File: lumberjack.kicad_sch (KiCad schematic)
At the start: 180 parts, among them J1 USB, J2 AVR_ISP_6, J3 JST, J4 JST, SW1 RESET, SW2 BOOT, U2 ATmega32A-P, Y1 16MHz

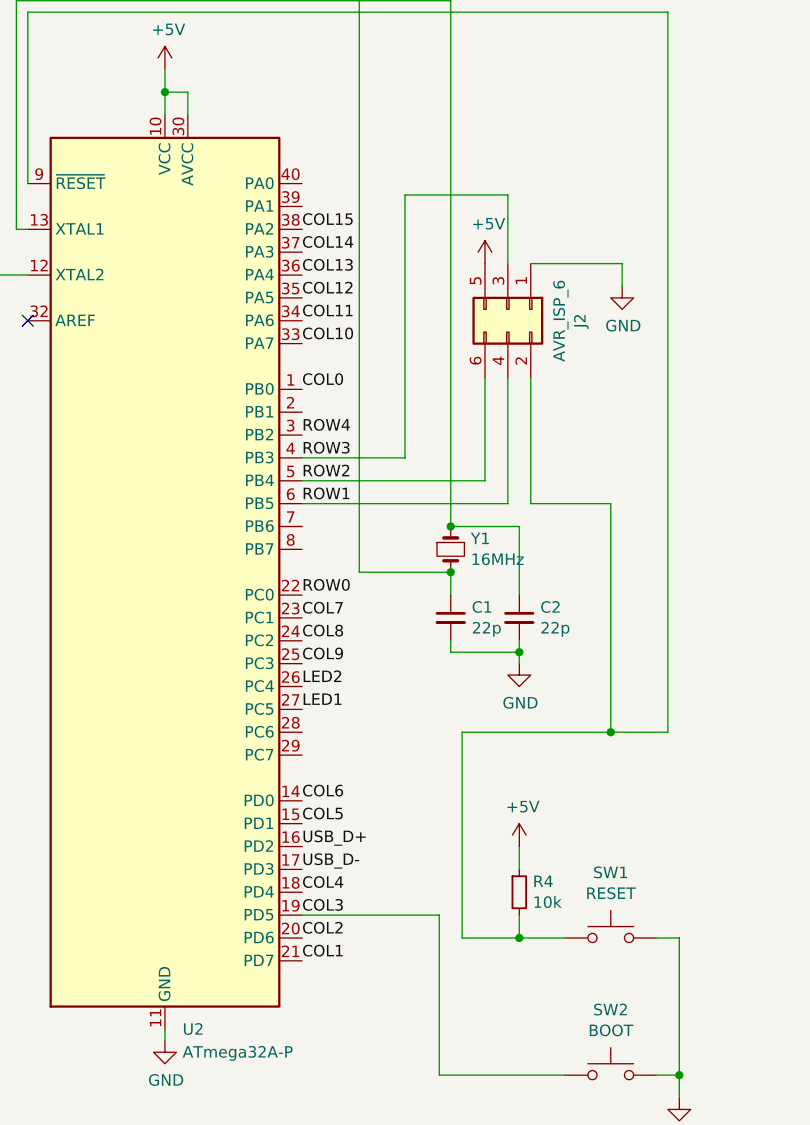
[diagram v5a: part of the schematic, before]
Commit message: middle part layout and traces
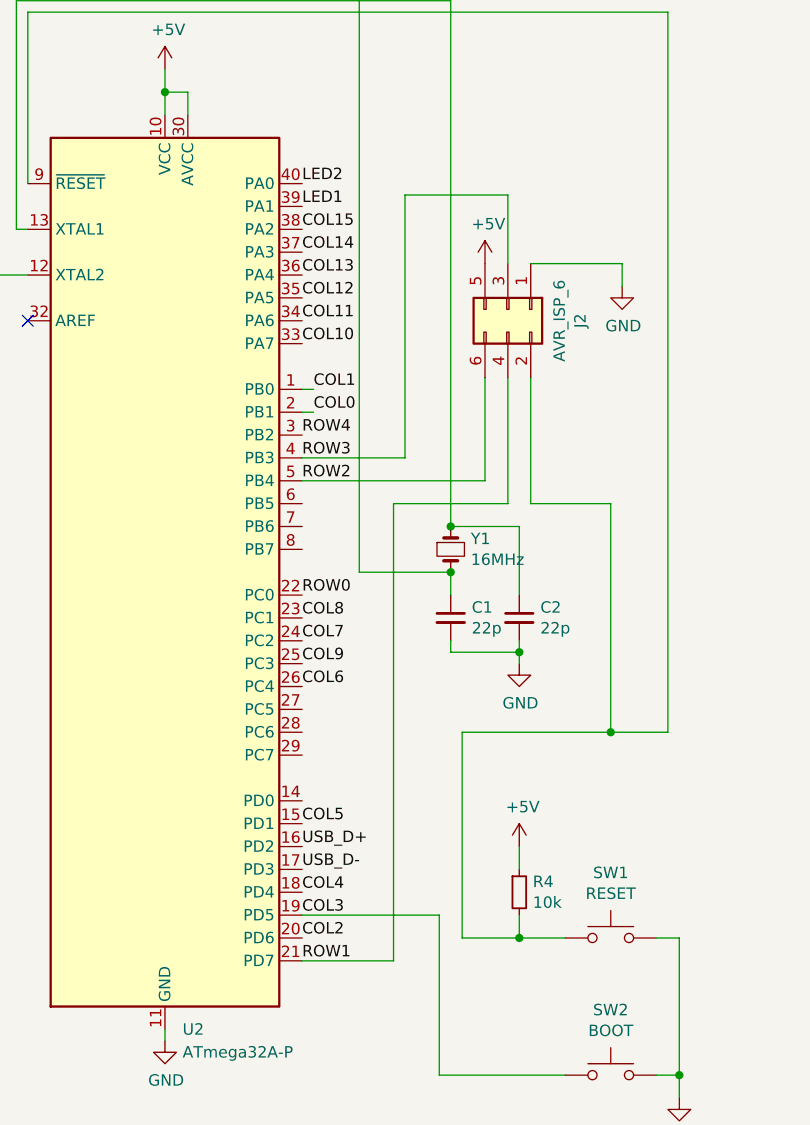
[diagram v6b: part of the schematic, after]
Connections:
- net COL0: now also U2.2 (PB1); no longer U2.1 (PB0)
- net COL1: now also U2.1 (PB0); no longer U2.21 (PD7)
- net COL6: now also U2.26 (PC4); no longer U2.14 (PD0)
- net COL7: now also U2.24 (PC2); no longer U2.23 (PC1)
- net COL8: now also U2.23 (PC1); no longer U2.24 (PC2)
- net LED1: now also U2.39 (PA1); no longer U2.27 (PC5)
- net LED2: now also U2.40 (PA0); no longer U2.26 (PC4)
- net ROW1: now also U2.21 (PD7); no longer U2.6 (PB5)
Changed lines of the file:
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@@
+    (stroke (width 0) (type default))
+  )
+  (wire (pts (xy 64.77 146.05) (xy 64.77 196.85))
     (stroke (width 0) (type default))
   )
@@
     (stroke (width 0) (type default))
   )
+  (wire (pts (xy 55.88 135.89) (xy 54.61 135.89))
+    (stroke (width 0) (type default))
+  )
   (wire (pts (xy 67.31 64.77) (xy 59.69 64.77))
     (stroke (width 0) (type default))
@@
     (stroke (width 0) (type default))
   )
-  (wire (pts (xy 54.61 146.05) (xy 77.47 146.05))
+  (wire (pts (xy 77.47 146.05) (xy 64.77 146.05))
     (stroke (width 0) (type default))
   )
@@
     (stroke (width 0) (type default))
   )
+  (wire (pts (xy 55.88 133.35) (xy 54.61 133.35))
+    (stroke (width 0) (type default))
+  )
   (wire (pts (xy 69.85 209.55) (xy 83.82 209.55))
     (stroke (width 0) (type default))
@@
   )
   (wire (pts (xy 302.26 74.93) (xy 302.26 92.71))
+    (stroke (width 0) (type default))
+  )
+  (wire (pts (xy 64.77 196.85) (xy 54.61 196.85))
     (stroke (width 0) (type default))
   )
@@
     (effects (font (size 1.27 1.27)) (justify left bottom))
   )
-  (label "COL1" (at 54.61 196.85 0) (fields_autoplaced)
+  (label "COL1" (at 55.88 133.35 0) (fields_autoplaced)
     (effects (font (size 1.27 1.27)) (justify left bottom))
   )
@@
     (effects (font (size 1.27 1.27)) (justify left bottom))
   )
-  (label "LED2" (at 54.61 166.37 0) (fields_autoplaced)
+  (label "LED2" (at 54.61 110.49 0) (fields_autoplaced)
     (effects (font (size 1.27 1.27)) (justify left bottom))
   )
@@
     (effects (font (size 1.27 1.27)) (justify left bottom))
   )
-  (label "LED1" (at 54.61 168.91 0) (fields_autoplaced)
+  (label "LED1" (at 54.61 113.03 0) (fields_autoplaced)
     (effects (font (size 1.27 1.27)) (justify left bottom))
   )
@@
     (effects (font (size 1.27 1.27)) (justify right bottom))
   )
-  (label "COL8" (at 54.61 161.29 0) (fields_autoplaced)
+  (label "COL8" (at 54.61 158.75 0) (fields_autoplaced)
     (effects (font (size 1.27 1.27)) (justify left bottom))
   )
@@
     (effects (font (size 1.27 1.27)) (justify left bottom))
   )
-  (label "COL6" (at 54.61 179.07 0) (fields_autoplaced)
+  (label "COL6" (at 54.61 166.37 0) (fields_autoplaced)
     (effects (font (size 1.27 1.27)) (justify left bottom))
   )
@@
     (effects (font (size 1.27 1.27)) (justify right bottom))
   )
-  (label "COL7" (at 54.61 158.75 0) (fields_autoplaced)
+  (label "COL7" (at 54.61 161.29 0) (fields_autoplaced)
     (effects (font (size 1.27 1.27)) (justify left bottom))
   )
@@
     (effects (font (size 1.27 1.27)) (justify left bottom))
   )
-  (label "ROW1" (at 54.61 146.05 0) (fields_autoplaced)
+  (label "ROW1" (at 54.61 196.85 0) (fields_autoplaced)
     (effects (font (size 1.27 1.27)) (justify left bottom))
   )
@@
     (effects (font (size 1.27 1.27)) (justify left bottom))
   )
-  (label "COL0" (at 54.61 133.35 0) (fields_autoplaced)
-    (effects (font (size 1.27 1.27)) (justify left bottom))
-  )
+  (label "COL0" (at 55.88 135.89 0) (fields_autoplaced)
+    (effects (font (size 1.27 1.27)) (justify left bottom))
+  )

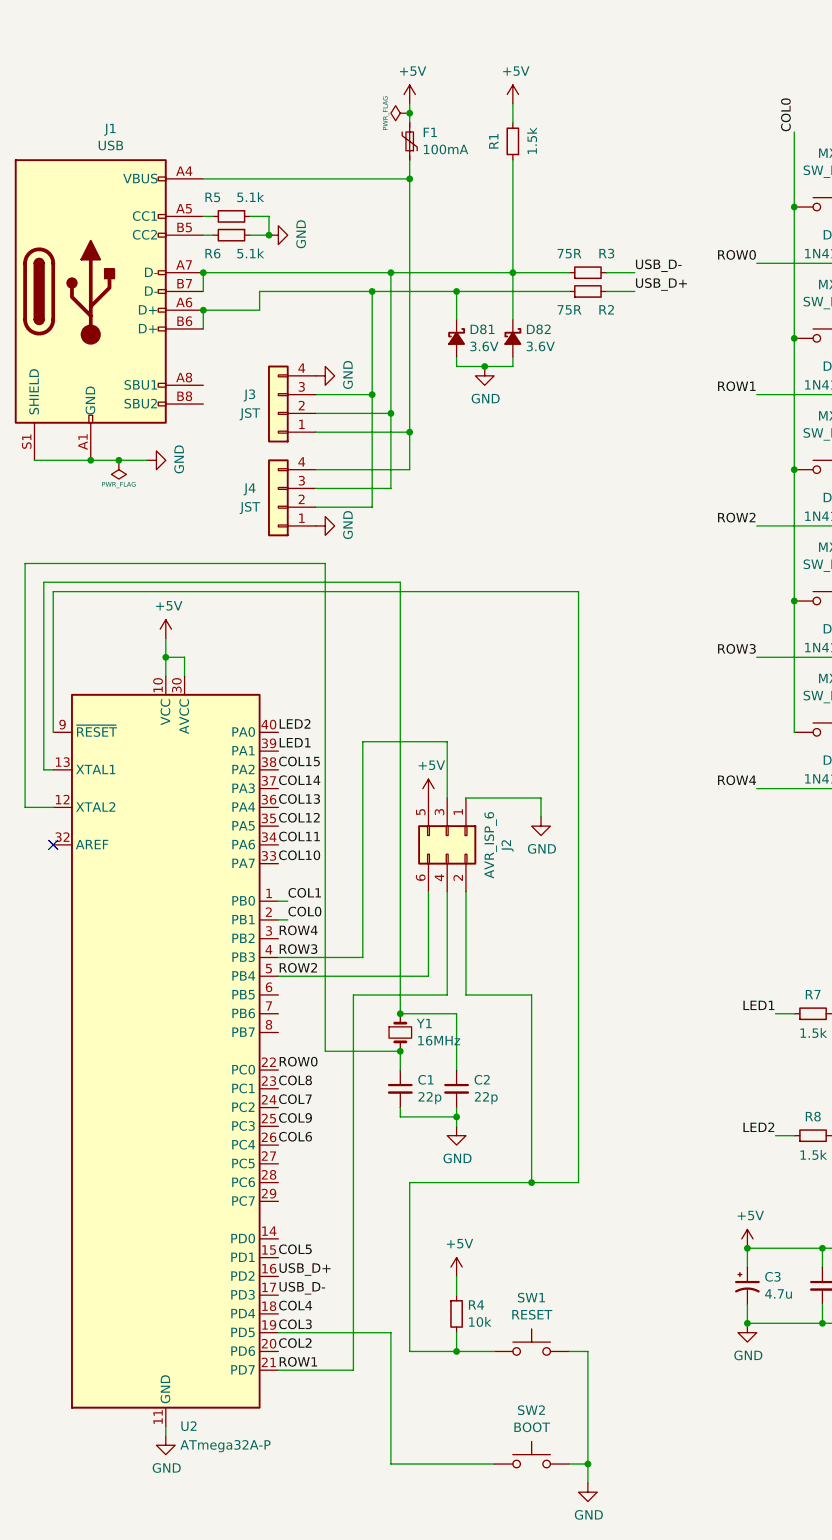
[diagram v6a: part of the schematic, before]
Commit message: usb mini and traces
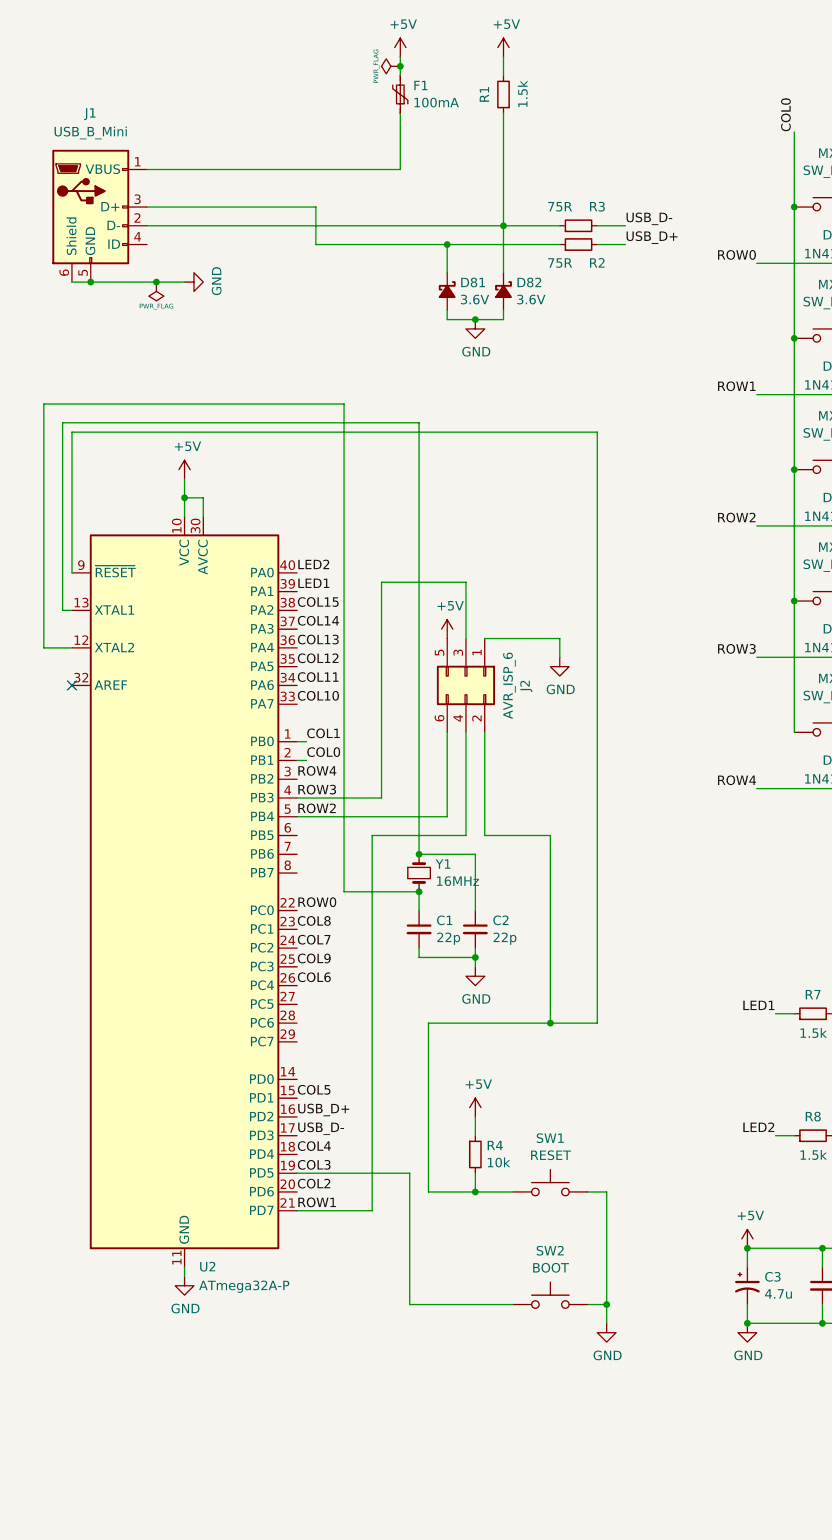
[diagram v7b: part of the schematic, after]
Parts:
- removed J1: USB, Connector_USB:USB_C_Receptacle_GCT_USB4085, symbol Connector:USB_C_Receptacle_USB2.0
- removed J3: JST, Connector_JST:JST_SH_SM04B-SRSS-TB_1x04-1MP_P1.00mm_Horizontal, symbol Connector_Generic:Conn_01x04
- removed J4: JST, lumberjack:S4B-ZRLFSN, symbol Connector_Generic:Conn_01x04
- removed R5, R6: 5.1k, Resistor_THT:R_Axial_DIN0204_L3.6mm_D1.6mm_P7.62mm_Horizontal, symbol Device:R_Small
- added J1: USB_B_Mini, lumberjack:USB_Mini-B, symbol Connector:USB_B_Mini
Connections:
- net GND: now also J1.5 (GND), J1.6 (Shield)
- net at D81.1 (K), R2.1: now also J1.3 (D+)
- net at D82.1 (K), R1.1, R3.1: now also J1.2 (D-)
- net at F1.1: now also J1.1 (VBUS)
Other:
- moved on the sheet: C1, C2, D81, D82, F1, J2, R1, R2, R3, R4, SW1, SW2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

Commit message: change dimensions to fit handrest
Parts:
- removed D1, D10, D11, D12, D13, D14, D15, D16, D17, D18, D19, D2, D20, D21, D22, D23, D24, D26, D27, D28, D29, D3, D30, D31, D32, D33, D34, D35, D36, D37, D38, D39, D4, D41, D42, D43, D44, D45, D46, D47, D48, D49, D5, D50, D51, D52, D53, D54, D55, D56, D57, D58, D59, D6, D60, D61, D62, D63, D64, D66, D67, D68, D69, D7, D71, D72, D73, D74, D75, D8, D9: 1N4148, Diode_THT:D_DO-35_SOD27_P7.62mm_Horizontal, symbol lumberjack-rescue:D_Small_ALT-Device
- removed H5, H6, H7: M2, lumberjack:MountingSlot_M2, symbol Mechanical:MountingHole
- removed J2: AVR_ISP_6, Connector_PinHeader_2.54mm:PinHeader_2x03_P2.54mm_Vertical, symbol Connector_Generic:Conn_02x03_Odd_Even
- removed MX1, MX11, MX12, MX13, MX14, MX16, MX17, MX18, MX19, MX21, MX22, MX23, MX24, MX26, MX27, MX28, MX29, MX31, MX32, MX33, MX34, MX36, MX37, MX38, MX39, MX41, MX42, MX43, MX44, MX46, MX47, MX48, MX49, MX51, MX52, MX53, MX54, MX56, MX57, MX58, MX6, MX61, MX62, MX64, MX66, MX68, MX69, MX72, MX73, MX74, MX75, MX8, MX9: SW_Push, lumberjack:MX, symbol Switch:SW_Push
- removed MX10, MX15, MX20, MX45, MX5, MX50, MX55, MX60: SW_Push, Button_Switch_Keyboard:SW_Cherry_MX_1.25u_PCB, symbol Switch:SW_Push
- removed MX2, MX67: SW_Push, Button_Switch_Keyboard:SW_Cherry_MX_1.50u_PCB, symbol Switch:SW_Push
- removed MX3, MX30, MX35: SW_Push, Button_Switch_Keyboard:SW_Cherry_MX_1.75u_PCB, symbol Switch:SW_Push
- removed MX4, MX63: SW_Push, Button_Switch_Keyboard:SW_Cherry_MX_2.25u_PCB, symbol Switch:SW_Push
- removed MX59: SW_Push, Button_Switch_Keyboard:SW_Cherry_MX_2.75u_PCB, symbol Switch:SW_Push
- removed MX7: SW_Push, lumberjack:MX_NTHSTH, symbol Switch:SW_Push
- removed MX71: SW_Push, Button_Switch_Keyboard:SW_Cherry_MX_2.00u_PCB, symbol Switch:SW_Push
- added D_0, D_1, D_10, D_11, D_12, D_13, D_14, D_15, D_16, D_17, D_18, D_19, D_2, D_20, D_21, D_22, D_23, D_24, D_25, D_26, D_27, D_28, D_29, D_3, D_30, D_31, D_32, D_33, D_34, D_35, D_36, D_37, D_38, D_39, D_4, D_40, D_41, D_42, D_43, D_44, D_45, D_46, D_47, D_48, D_49, D_5, D_50, D_51, D_52, D_53, D_54, D_55, D_56, D_57, D_58, D_59, D_6, D_60, D_61, D_62, D_63, D_64, D_65, D_7, D_8, D_9: 1N4148, Diode_THT:D_DO-35_SOD27_P7.62mm_Horizontal, symbol Device:D_Small
- added K_0, K_1, K_10, K_11, K_12, K_13, K_14, K_16, K_17, K_18, K_19, K_2, K_20, K_21, K_22, K_23, K_24, K_25, K_26, K_27, K_3, K_30, K_31, K_32, K_33, K_34, K_35, K_36, K_37, K_38, K_39, K_4, K_40, K_43, K_44, K_45, K_46, K_47, K_48, K_49, K_5, K_50, K_51, K_52, K_6, K_62, K_63, K_64, K_65, K_7, K_8, K_9: KEYSW, Button_Switch_Keyboard:SW_Cherry_MX_1.00u_PCB, symbol MX_Alps_Hybrid:MX-NoLED
- added K_15, K_28: KEYSW, Button_Switch_Keyboard:SW_Cherry_MX_1.50u_PCB, symbol MX_Alps_Hybrid:MX-NoLED
- added K_29, K_58, K_59: KEYSW, Button_Switch_Keyboard:SW_Cherry_MX_1.75u_PCB, symbol MX_Alps_Hybrid:MX-NoLED
- added K_41, K_42: KEYSW, Button_Switch_Keyboard:SW_Cherry_MX_2.25u_PCB, symbol MX_Alps_Hybrid:MX-NoLED
- added K_53: KEYSW, Button_Switch_Keyboard:SW_Cherry_MX_2.75u_PCB, symbol MX_Alps_Hybrid:MX-NoLED
- added K_54, K_55, K_56, K_57, K_60, K_61: KEYSW, Button_Switch_Keyboard:SW_Cherry_MX_1.25u_PCB, symbol MX_Alps_Hybrid:MX-NoLED
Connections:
- net COL0: now also U2.1 (PB0), K_0.1 (COL), K_15.1 (COL), K_29.1 (COL), K_42.1 (COL), K_54.1 (COL); no longer U2.2 (PB1)
- net COL1: now also U2.2 (PB1), K_1.1 (COL), K_16.1 (COL), K_30.1 (COL), K_43.1 (COL), K_55.1 (COL); no longer U2.1 (PB0)
- net COL10: now also U2.26 (PC4), K_10.1 (COL), K_25.1 (COL), K_39.1 (COL), K_52.1 (COL), K_62.1 (COL); no longer U2.33 (PA7)
- net COL11: now also U2.25 (PC3), K_11.1 (COL), K_26.1 (COL), K_40.1 (COL), K_53.1 (COL), K_63.1 (COL); no longer U2.34 (PA6)
- net COL12: now also U2.24 (PC2), K_12.1 (COL), K_27.1 (COL), K_41.1 (COL), K_64.1 (COL); no longer U2.35 (PA5)
- net COL13: now also U2.23 (PC1), K_13.1 (COL), K_28.1 (COL), K_65.1 (COL); no longer U2.36 (PA4)
- net COL14: now also U2.22 (PC0), K_14.1 (COL); no longer U2.37 (PA3)
- net COL15: now also U2.21 (PD7); no longer U2.38 (PA2)
- net COL2: now also U2.3 (PB2), K_17.1 (COL), K_2.1 (COL), K_31.1 (COL), K_44.1 (COL), K_56.1 (COL); no longer U2.20 (PD6)
- net COL3: now also U2.4 (PB3), K_18.1 (COL), K_3.1 (COL), K_32.1 (COL), K_45.1 (COL), K_57.1 (COL); no longer U2.19 (PD5)
- net COL4: now also U2.5 (PB4), K_19.1 (COL), K_33.1 (COL), K_4.1 (COL), K_46.1 (COL); no longer U2.18 (PD4)
- net COL5: now also U2.6 (PB5), K_20.1 (COL), K_34.1 (COL), K_47.1 (COL), K_5.1 (COL), K_58.1 (COL); no longer U2.15 (PD1)
- net COL6: now also U2.33 (PA7), K_21.1 (COL), K_35.1 (COL), K_48.1 (COL), K_59.1 (COL), K_6.1 (COL); no longer U2.26 (PC4)
- net COL7: now also U2.29 (PC7), K_22.1 (COL), K_36.1 (COL), K_49.1 (COL), K_7.1 (COL); no longer U2.24 (PC2)
- net COL8: now also U2.28 (PC6), K_23.1 (COL), K_37.1 (COL), K_50.1 (COL), K_60.1 (COL), K_8.1 (COL); no longer U2.23 (PC1)
- net COL9: now also U2.27 (PC5), K_24.1 (COL), K_38.1 (COL), K_51.1 (COL), K_61.1 (COL), K_9.1 (COL); no longer U2.25 (PC3)
- net LED1: now also U2.40 (PA0); no longer U2.39 (PA1)
- net LED2: now also U2.39 (PA1); no longer U2.40 (PA0)
- net ROW0: now also U2.37 (PA3), D_0.1 (K), D_1.1 (K), D_10.1 (K), D_11.1 (K), D_12.1 (K), D_13.1 (K), D_14.1 (K), D_2.1 (K), D_3.1 (K), D_4.1 (K), D_5.1 (K), D_6.1 (K), D_7.1 (K), D_8.1 (K), D_9.1 (K); no longer U2.22 (PC0)
- net ROW1: now also U2.38 (PA2), D_15.1 (K), D_16.1 (K), D_17.1 (K), D_18.1 (K), D_19.1 (K), D_20.1 (K), D_21.1 (K), D_22.1 (K), D_23.1 (K), D_24.1 (K), D_25.1 (K), D_26.1 (K), D_27.1 (K), D_28.1 (K); no longer U2.21 (PD7)
- net ROW2: now also U2.18 (PD4), D_29.1 (K), D_30.1 (K), D_31.1 (K), D_32.1 (K), D_33.1 (K), D_34.1 (K), D_35.1 (K), D_36.1 (K), D_37.1 (K), D_38.1 (K), D_39.1 (K), D_40.1 (K), D_41.1 (K); no longer U2.5 (PB4)
- net ROW3: now also U2.19 (PD5), D_42.1 (K), D_43.1 (K), D_44.1 (K), D_45.1 (K), D_46.1 (K), D_47.1 (K), D_48.1 (K), D_49.1 (K), D_50.1 (K), D_51.1 (K), D_52.1 (K), D_53.1 (K); no longer U2.3 (PB2), U2.4 (PB3)
- new net: D_10.2 (A), K_10.2 (ROW)
- new net: D_54.2 (A), K_54.2 (ROW)
- new net: D_37.2 (A), K_37.2 (ROW)
- new net: D_0.2 (A), K_0.2 (ROW)
- new net: D_55.2 (A), K_55.2 (ROW)
- new net: D_41.2 (A), K_41.2 (ROW)
- new net: D_3.2 (A), K_3.2 (ROW)
- new net: D_60.2 (A), K_60.2 (ROW)
- new net: D_27.2 (A), K_27.2 (ROW)
- new net: D_63.2 (A), K_63.2 (ROW)
- new net: D_16.2 (A), K_16.2 (ROW)
- new net: D_49.2 (A), K_49.2 (ROW)
- new net: D_59.2 (A), K_59.2 (ROW)
- new net: D_43.2 (A), K_43.2 (ROW)
- new net: D_22.2 (A), K_22.2 (ROW)
- new net: D_18.2 (A), K_18.2 (ROW)
- new net: D_32.2 (A), K_32.2 (ROW)
- new net: D_19.2 (A), K_19.2 (ROW)
- new net: D_6.2 (A), K_6.2 (ROW)
- new net: D_7.2 (A), K_7.2 (ROW)
- new net: D_50.2 (A), K_50.2 (ROW)
- new net: D_26.2 (A), K_26.2 (ROW)
- new net: D_28.2 (A), K_28.2 (ROW)
- new net: D_61.2 (A), K_61.2 (ROW)
- new net: D_57.2 (A), K_57.2 (ROW)
- new net: D_5.2 (A), K_5.2 (ROW)
- new net: D_56.2 (A), K_56.2 (ROW)
- new net: D_47.2 (A), K_47.2 (ROW)
- new net: D_38.2 (A), K_38.2 (ROW)
- new net: D_52.2 (A), K_52.2 (ROW)
- new net: D_45.2 (A), K_45.2 (ROW)
- new net: D_20.2 (A), K_20.2 (ROW)
- new net: D_13.2 (A), K_13.2 (ROW)
- new net: D_2.2 (A), K_2.2 (ROW)
- new net: D_46.2 (A), K_46.2 (ROW)
- new net: D_64.2 (A), K_64.2 (ROW)
- new net: D_44.2 (A), K_44.2 (ROW)
- new net: D_8.2 (A), K_8.2 (ROW)
- new net: D_17.2 (A), K_17.2 (ROW)
- new net: D_48.2 (A), K_48.2 (ROW)
- new net: D_42.2 (A), K_42.2 (ROW)
- new net: D_9.2 (A), K_9.2 (ROW)
- new net: D_31.2 (A), K_31.2 (ROW)
- new net: D_58.2 (A), K_58.2 (ROW)
- new net: D_23.2 (A), K_23.2 (ROW)
- new net: D_33.2 (A), K_33.2 (ROW)
- new net: D_65.2 (A), K_65.2 (ROW)
- new net: D_4.2 (A), K_4.2 (ROW)
- new net: D_39.2 (A), K_39.2 (ROW)
- new net: D_15.2 (A), K_15.2 (ROW)
- new net: D_35.2 (A), K_35.2 (ROW)
- new net: D_53.2 (A), K_53.2 (ROW)
- new net: D_12.2 (A), K_12.2 (ROW)
- new net: D_40.2 (A), K_40.2 (ROW)
- new net: D_11.2 (A), K_11.2 (ROW)
- new net: D_51.2 (A), K_51.2 (ROW)
- new net: D_14.2 (A), K_14.2 (ROW)
- new net: D_25.2 (A), K_25.2 (ROW)
- new net: D_62.2 (A), K_62.2 (ROW)
- new net: D_29.2 (A), K_29.2 (ROW)
- new net: D_36.2 (A), K_36.2 (ROW)
- new net: D_30.2 (A), K_30.2 (ROW)
- new net: D_1.2 (A), K_1.2 (ROW)
- new net: D_21.2 (A), K_21.2 (ROW)
- new net: D_34.2 (A), K_34.2 (ROW)
- new net: D_24.2 (A), K_24.2 (ROW)
- new net ROW4: D_54.1 (K), D_55.1 (K), D_56.1 (K), D_57.1 (K), D_58.1 (K), D_59.1 (K), D_60.1 (K), D_61.1 (K), D_62.1 (K), D_63.1 (K), D_64.1 (K), D_65.1 (K), U2.20 (PD6)
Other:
- moved on the sheet: H11, H12, H8, H9
